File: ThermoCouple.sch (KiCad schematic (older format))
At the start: 11 parts, among them U2 MCP3550-60-E/SN, U3 MCP3550-60-E/SN, U4 LM324

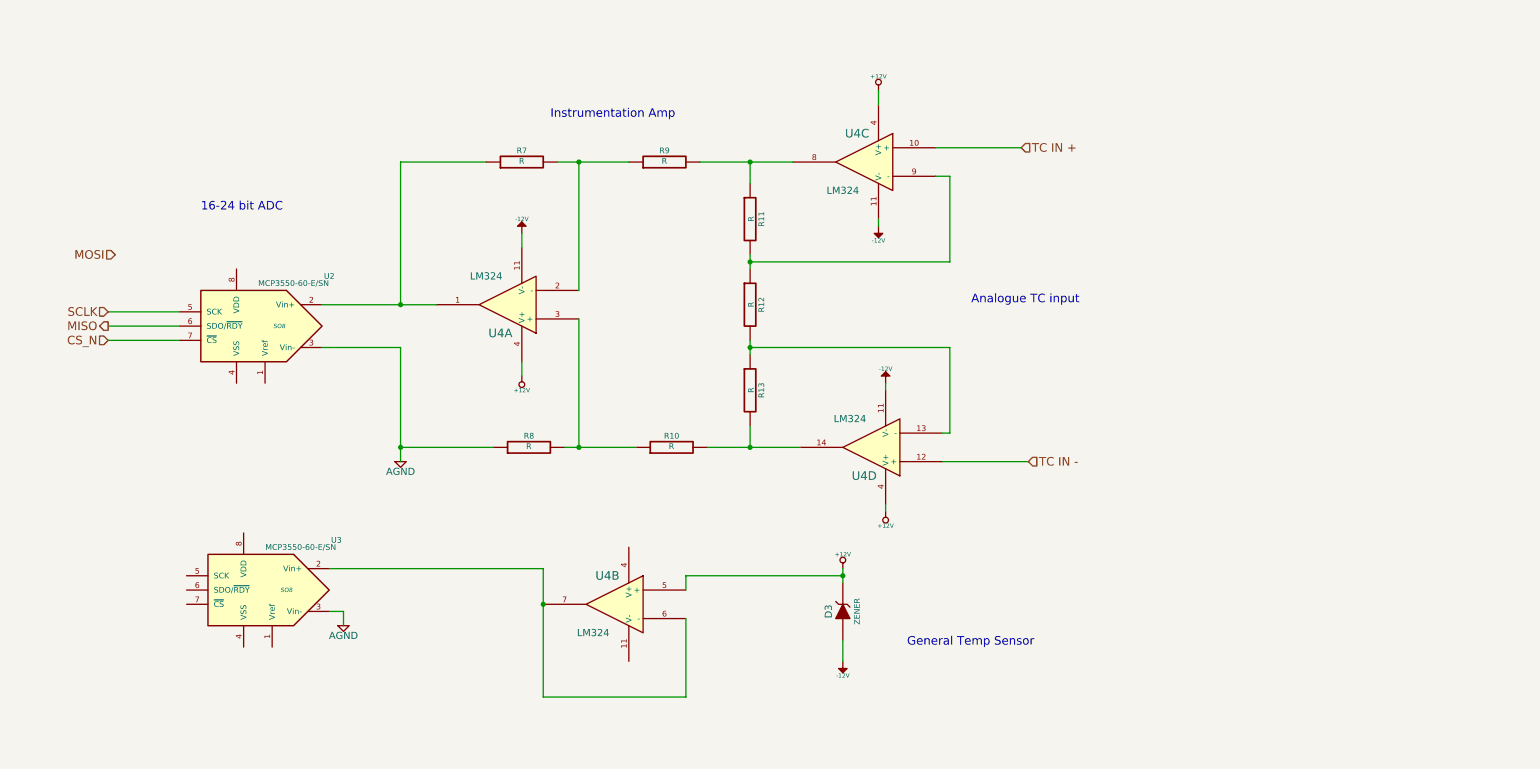
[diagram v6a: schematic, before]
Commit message: Associated Thermocouple module
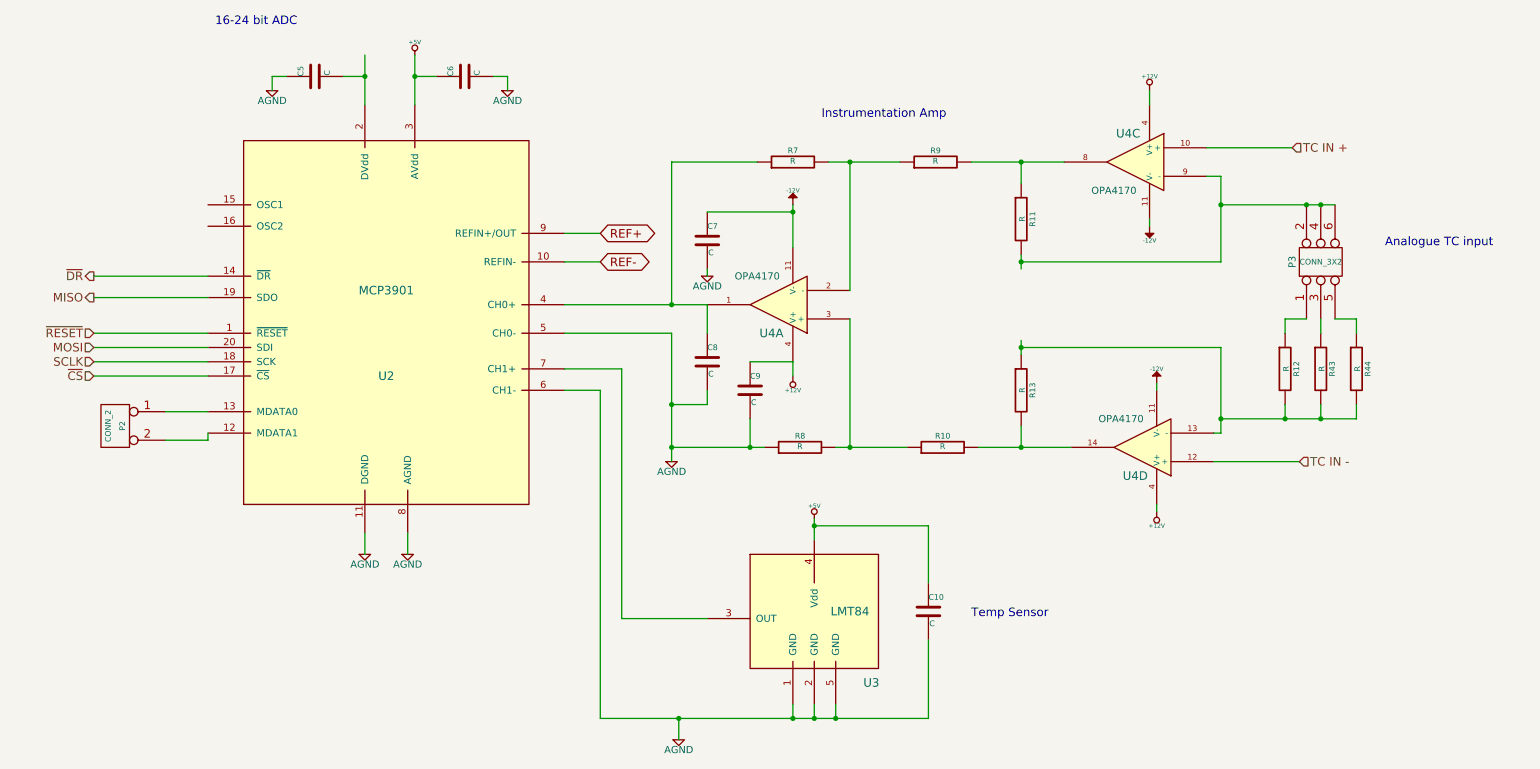
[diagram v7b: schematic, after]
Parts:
- removed D3: ZENER, ~, symbol ZENER
- removed U2, U3: MCP3550-60-E/SN, SO8, symbol MCP3550-60-E/SN
- removed unit 2 of U4
- added C10, C5, C6, C7, C8, C9: C, symbol C
- added P2: CONN_2, symbol CONN_2
- added P3: CONN_3X2, symbol CONN_3X2
- added R43, R44: R, ~, symbol R
- added U2: MCP3901, symbol MCP3901
- added U3: LMT84, symbol LMT84
- U4: value LM324 -> OPA4170; MFG Part Number (none) -> OPA4170
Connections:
- net labels added: +5V, REF+, REF-, ~CS, ~DR, ~RESET
- net labels removed: CS_N
- wire segments 43 -> 82
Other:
- note added: "Temp Sensor"
- note removed: "General Temp Sensor"
- moved on the sheet: R10, R11, R12, R13, R7, R8, R9, U4A, U4C, U4D

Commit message: place thermocouple components
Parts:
- added R47, R48: 0, symbol R
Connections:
- net labels added: CH0+, CH0-, CH1+, CH1-
- wire segments 82 -> 84
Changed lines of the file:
@@
 	6350 3500 6350 3400
 Wire Wire Line
-	5500 3200 5500 4100
+	5500 3800 5500 4100
 Wire Wire Line
 	5500 2000 5500 3000
@@
 	5750 3000 5750 3200
 Wire Wire Line
-	5750 3600 5750 3700
-Wire Wire Line
-	5750 3700 5500 3700
-Connection ~ 5500 3700
+	5750 3600 5750 3900
+Wire Wire Line
+	5750 3900 5500 3900
+Connection ~ 5500 3900
 $Comp
 L R R43
@@
 	4750 3600 5000 3600
 Wire Wire Line
-	5000 3600 5000 5900
-Wire Wire Line
 	5000 5900 7300 5900
 Wire Wire Line
@@
 	2700 1400 2700 1500
 Wire Wire Line
-	3350 1600 3350 1250
+	3350 1250 3350 1600
 Wire Wire Line
 	3200 1400 3350 1400
@@
 Wire Wire Line
 	2250 3950 2250 3900
+Text Label 4950 3000 0    60   ~ 0
+CH0+
+Text Label 4950 3200 0    60   ~ 0
+CH0-
+Text Label 4950 3450 0    60   ~ 0
+CH1+
+Text Label 4950 3600 0    60   ~ 0
+CH1-
+$Comp
+L R R47
+U 1 1 530388D9
+P 5000 4650
+F 0 "R47" V 5080 4650 40  0000 C CNN
+F 1 "0" V 5007 4651 40  0000 C CNN
+F 2 "" V 4930 4650 30  0000 C CNN
+F 3 "" H 5000 4650 30  0000 C CNN
+	1    5000 4650
+	1    0    0    -1
+$EndComp
+Wire Wire Line
+	5000 3600 5000 4400
+Wire Wire Line
+	5000 4900 5000 5900
+$Comp
+L R R48
+U 1 1 53038A46
+P 5500 3550
+F 0 "R48" V 5580 3550 40  0000 C CNN
+F 1 "0" V 5507 3551 40  0000 C CNN
+F 2 "" V 5430 3550 30  0000 C CNN
+F 3 "" H 5500 3550 30  0000 C CNN
+	1    5500 3550
+	1    0    0    -1
+$EndComp
+Wire Wire Line
+	5500 3200 5500 3300
 $EndSCHEMATC
